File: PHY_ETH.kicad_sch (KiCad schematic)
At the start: 15 parts, among them U8 LAN8742A, Y1 LFXTAL071758Cutt

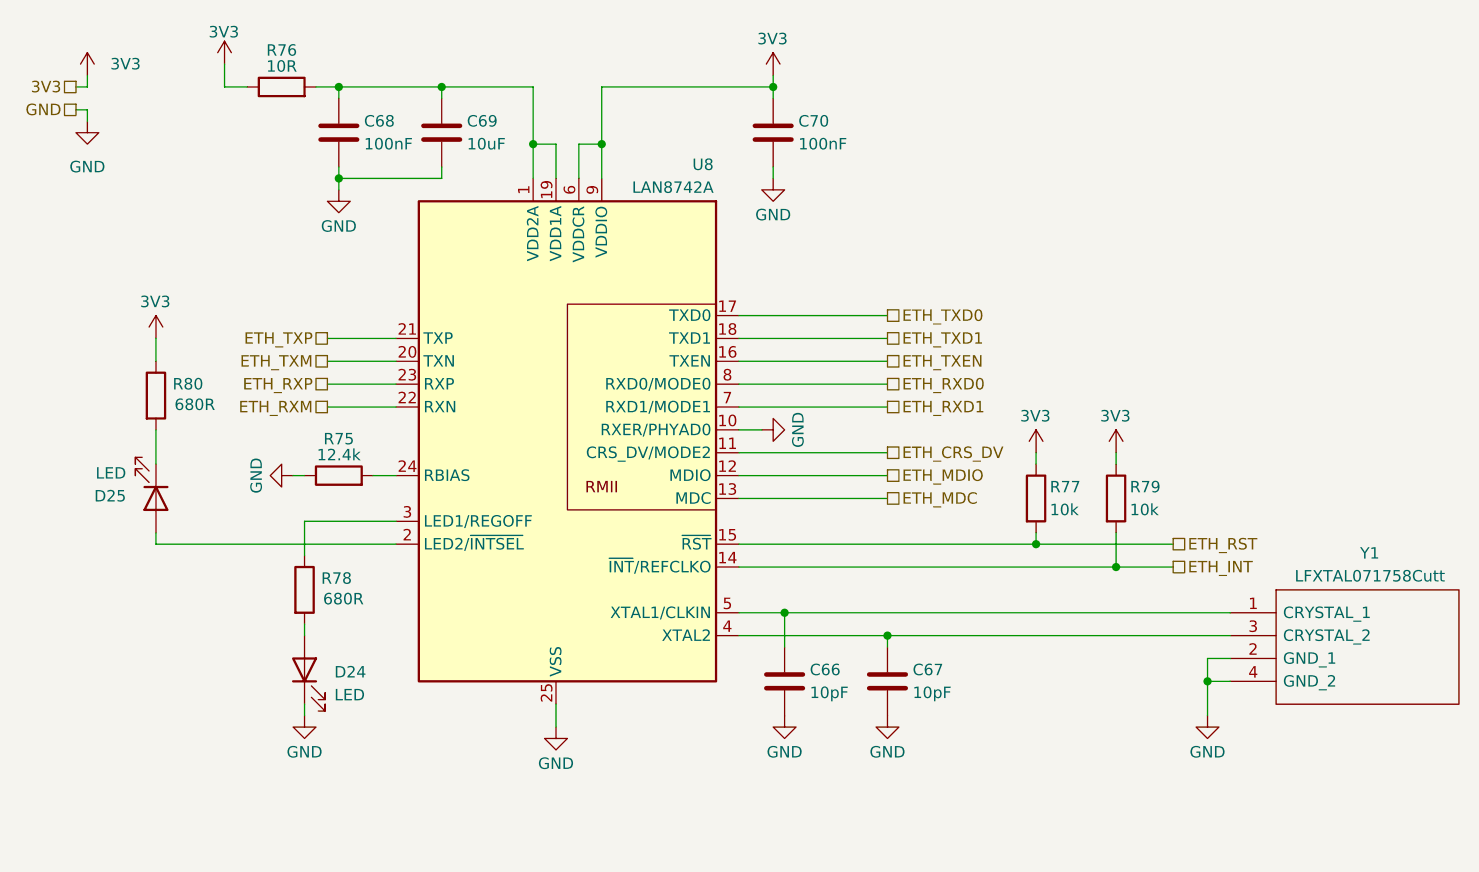
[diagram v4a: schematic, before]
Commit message: redid annotations, added test point
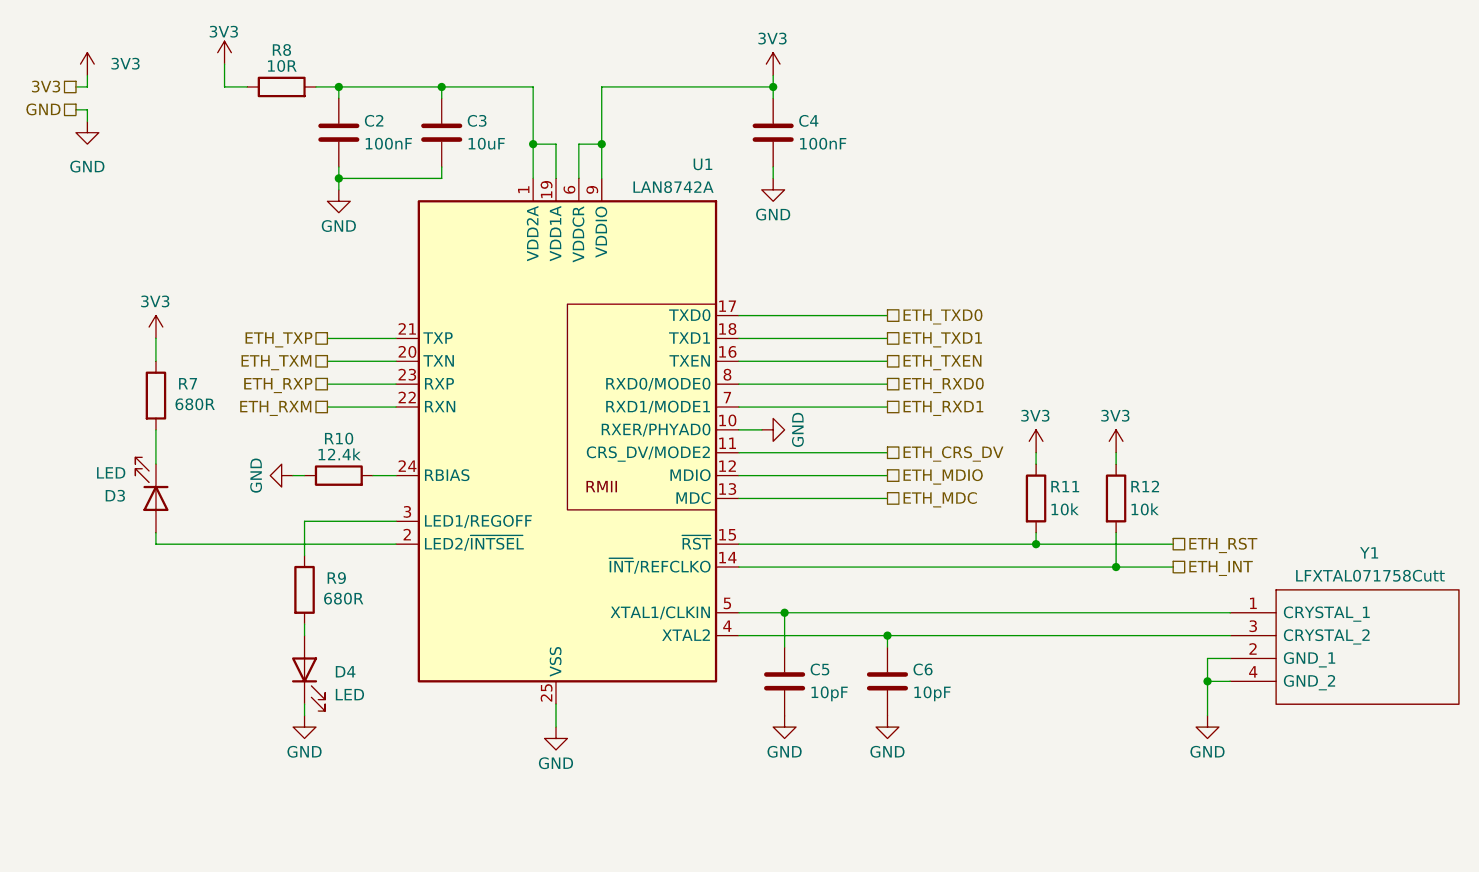
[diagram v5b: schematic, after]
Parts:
- C6: renamed from C67; footprint (none) -> Capacitor_SMD:C_0603_1608Metric_Pad1.08x0.95mm_HandSolder
- renumbered C68 to C2, C69 to C3, C70 to C4, C66 to C5, D25 to D3, D24 to D4, R75 to R10, R77 to R11, R79 to R12, R80 to R7, R76 to R8, R78 to R9, U8 to U1
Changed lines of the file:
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@@
 		(on_board yes)
 		(dnp no)
-		(property "Reference" "R79"
+		(property "Reference" "R12"
 			(at 142.494 69.85 0)
 			(effects
@@
 			(project "NCU"
 				(path "/3aee14c3-5480-4f7c-989e-3fef81779034/9758cbcc-2ab2-405c-935d-3964f8470771"
-					(reference "R79")
+					(reference "R12")
 					(unit 1)
 				)
@@
 		(on_board yes)
 		(dnp no)
-		(property "Reference" "R80"
+		(property "Reference" "R7"
 			(at 37.846 58.42 0)
 			(effects
@@
 			(project "NCU"
 				(path "/3aee14c3-5480-4f7c-989e-3fef81779034/9758cbcc-2ab2-405c-935d-3964f8470771"
-					(reference "R80")
+					(reference "R7")
 					(unit 1)
 				)
@@
 		(on_board yes)
 		(dnp no)
-		(property "Reference" "D24"
+		(property "Reference" "D4"
 			(at 54.102 90.424 90)
 			(effects
@@
 			(project "NCU"
 				(path "/3aee14c3-5480-4f7c-989e-3fef81779034/9758cbcc-2ab2-405c-935d-3964f8470771"
-					(reference "D24")
+					(reference "D4")
 					(unit 1)
 				)
@@
 		(on_board yes)
 		(dnp no)
-		(property "Reference" "R78"
+		(property "Reference" "R9"
 			(at 54.356 80.01 0)
 			(effects
@@
 			(project "NCU"
 				(path "/3aee14c3-5480-4f7c-989e-3fef81779034/9758cbcc-2ab2-405c-935d-3964f8470771"
-					(reference "R78")
+					(reference "R9")
 					(unit 1)
 				)
@@
 		(on_board yes)
 		(dnp no)
-		(property "Reference" "#PWR0237"
+		(property "Reference" "#PWR0100"
 			(at 151.13 101.6 0)
 			(effects
@@
 			(project "NCU"
 				(path "/3aee14c3-5480-4f7c-989e-3fef81779034/9758cbcc-2ab2-405c-935d-3964f8470771"
-					(reference "#PWR0237")
+					(reference "#PWR0100")
 					(unit 1)
 				)
@@
 		(on_board yes)
 		(dnp no)
-		(property "Reference" "C70"
+		(property "Reference" "C4"
 			(at 105.664 29.21 0)
 			(effects
@@
 			(project "NCU"
 				(path "/3aee14c3-5480-4f7c-989e-3fef81779034/9758cbcc-2ab2-405c-935d-3964f8470771"
-					(reference "C70")
+					(reference "C4")
 					(unit 1)
 				)
@@
 		(on_board yes)
 		(dnp no)
-		(property "Reference" "#PWR0241"
+		(property "Reference" "#PWR091"
 			(at 54.61 43.18 0)
 			(effects
@@
 			(project "NCU"
 				(path "/3aee14c3-5480-4f7c-989e-3fef81779034/9758cbcc-2ab2-405c-935d-3964f8470771"
-					(reference "#PWR0241")
+					(reference "#PWR091")
 					(unit 1)
 				)
@@
 		(on_board yes)
 		(dnp no)
-		(property "Reference" "#PWR0238"
+		(property "Reference" "#PWR096"
 			(at 104.14 101.6 0)
 			(effects
@@
 			(project "NCU"
 				(path "/3aee14c3-5480-4f7c-989e-3fef81779034/9758cbcc-2ab2-405c-935d-3964f8470771"
-					(reference "#PWR0238")
+					(reference "#PWR096")
 					(unit 1)
 				)
@@
 		(on_board yes)
 		(dnp no)
-		(property "Reference" "#PWR0240"
+		(property "Reference" "#PWR088"
 			(at 41.91 26.67 0)
 			(effects
@@
 			(project "NCU"
 				(path "/3aee14c3-5480-4f7c-989e-3fef81779034/9758cbcc-2ab2-405c-935d-3964f8470771"
-					(reference "#PWR0240")
+					(reference "#PWR088")
 					(unit 1)
 				)
@@
 		(on_board yes)
 		(dnp no)
-		(property "Reference" "#PWR0234"
+		(property "Reference" "#PWR092"
 			(at 78.74 102.87 0)
 			(effects
@@
 			(project "NCU"
 				(path "/3aee14c3-5480-4f7c-989e-3fef81779034/9758cbcc-2ab2-405c-935d-3964f8470771"
-					(reference "#PWR0234")
+					(reference "#PWR092")
 					(unit 1)
 				)
@@
 		(on_board yes)
 		(dnp no)
-		(property "Reference" "C68"
+		(property "Reference" "C2"
 			(at 57.404 29.21 0)
 			(effects
@@
 			(project "NCU"
 				(path "/3aee14c3-5480-4f7c-989e-3fef81779034/9758cbcc-2ab2-405c-935d-3964f8470771"
-					(reference "C68")
+					(reference "C2")
 					(unit 1)
 				)
@@
 		(on_board yes)
 		(dnp no)
-		(property "Reference" "C67"
+		(property "Reference" "C6"
 			(at 118.364 90.17 0)
 			(effects
@@
 			)
 		)
-		(property "Footprint" ""
+		(property "Footprint" "Capacitor_SMD:C_0603_1608Metric_Pad1.08x0.95mm_HandSolder"
 			(at 116.5352 95.25 0)
 			(effects
@@
 			(project "NCU"
 				(path "/3aee14c3-5480-4f7c-989e-3fef81779034/9758cbcc-2ab2-405c-935d-3964f8470771"
-					(reference "C67")
+					(reference "C6")
 					(unit 1)
 				)
@@
 		(on_board yes)
 		(dnp no)
-		(property "Reference" "U8"
+		(property "Reference" "U1"
 			(at 96.266 34.036 0)
 			(effects
@@
 			(project "NCU"
 				(path "/3aee14c3-5480-4f7c-989e-3fef81779034/9758cbcc-2ab2-405c-935d-3964f8470771"
-					(reference "U8")
+					(reference "U1")
 					(unit 1)
 				)
@@
 		(on_board yes)
 		(dnp no)
-		(property "Reference" "D25"
+		(property "Reference" "D3"
 			(at 30.988 70.866 90)
 			(effects
@@
 			(project "NCU"
 				(path "/3aee14c3-5480-4f7c-989e-3fef81779034/9758cbcc-2ab2-405c-935d-3964f8470771"
-					(reference "D25")
+					(reference "D3")
 					(unit 1)
 				)
@@
 		(on_board yes)
 		(dnp no)
-		(property "Reference" "R76"
+		(property "Reference" "R8"
 			(at 48.26 21.336 90)
 			(effects
@@
 			(project "NCU"
 				(path "/3aee14c3-5480-4f7c-989e-3fef81779034/9758cbcc-2ab2-405c-935d-3964f8470771"
-					(reference "R76")
+					(reference "R8")
 					(unit 1)
 				)
@@
 		(on_board yes)
 		(dnp no)
-		(property "Reference" "R77"
+		(property "Reference" "R11"
 			(at 133.604 69.85 0)
 			(effects
@@
 			(project ""
 				(path "/3aee14c3-5480-4f7c-989e-3fef81779034/9758cbcc-2ab2-405c-935d-3964f8470771"
-					(reference "R77")
+					(reference "R11")
 					(unit 1)
 				)
@@
 		(on_board yes)
 		(dnp no)
-		(property "Reference" "C69"
+		(property "Reference" "C3"
 			(at 68.834 29.21 0)
 			(effects
@@
 			(project "NCU"
 				(path "/3aee14c3-5480-4f7c-989e-3fef81779034/9758cbcc-2ab2-405c-935d-3964f8470771"
-					(reference "C69")
+					(reference "C3")
 					(unit 1)
 				)
@@
 		(on_board yes)
 		(dnp no)
-		(property "Reference" "#PWR0242"
+		(property "Reference" "#PWR098"
 			(at 132.08 69.85 0)
 			(effects
@@
 			(project "NCU"
 				(path "/3aee14c3-5480-4f7c-989e-3fef81779034/9758cbcc-2ab2-405c-935d-3964f8470771"
-					(reference "#PWR0242")
+					(reference "#PWR098")
 					(unit 1)
 				)
@@
 		(on_board yes)
 		(dnp no)
-		(property "Reference" "#PWR0243"
+		(property "Reference" "#PWR090"
 			(at 50.8 101.6 0)
 			(effects
@@
 			(project "NCU"
 				(path "/3aee14c3-5480-4f7c-989e-3fef81779034/9758cbcc-2ab2-405c-935d-3964f8470771"
-					(reference "#PWR0243")
+					(reference "#PWR090")
 					(unit 1)
 				)
@@
 		(on_board yes)
 		(dnp no)
-		(property "Reference" "#PWR0244"
+		(property "Reference" "#PWR099"
 			(at 140.97 69.85 0)
 			(effects
@@
 			(project "NCU"
 				(path "/3aee14c3-5480-4f7c-989e-3fef81779034/9758cbcc-2ab2-405c-935d-3964f8470771"
-					(reference "#PWR0244")
+					(reference "#PWR099")
 					(unit 1)
 				)
@@
 		(dnp no)
 		(fields_autoplaced yes)
-		(property "Reference" "#PWR0115"
+		(property "Reference" "#PWR086"
 			(at 26.67 35.56 0)
 			(effects
@@
 			(project "NCU"
 				(path "/3aee14c3-5480-4f7c-989e-3fef81779034/9758cbcc-2ab2-405c-935d-3964f8470771"
-					(reference "#PWR0115")
+					(reference "#PWR086")
 					(unit 1)
 				)
@@
 		(on_board yes)
 		(dnp no)
-		(property "Reference" "#PWR0235"
+		(property "Reference" "#PWR094"
 			(at 102.87 27.94 0)
 			(effects
@@
 			(project "NCU"
 				(path "/3aee14c3-5480-4f7c-989e-3fef81779034/9758cbcc-2ab2-405c-935d-3964f8470771"
-					(reference "#PWR0235")
+					(reference "#PWR094")
 					(unit 1)
 				)
@@
 		(on_board yes)
 		(dnp no)
-		(property "Reference" "#PWR0246"
+		(property "Reference" "#PWR087"
 			(at 34.29 57.15 0)
 			(effects
@@
 			(project "NCU"
 				(path "/3aee14c3-5480-4f7c-989e-3fef81779034/9758cbcc-2ab2-405c-935d-3964f8470771"
-					(reference "#PWR0246")
+					(reference "#PWR087")
 					(unit 1)
 				)
@@
 		(on_board yes)
 		(dnp no)
-		(property "Reference" "#PWR0236"
+		(property "Reference" "#PWR089"
 			(at 43.18 68.58 0)
 			(effects
@@
 			(project "NCU"
 				(path "/3aee14c3-5480-4f7c-989e-3fef81779034/9758cbcc-2ab2-405c-935d-3964f8470771"
-					(reference "#PWR0236")
+					(reference "#PWR089")
 					(unit 1)
 				)
@@
 		(on_board yes)
 		(dnp no)
-		(property "Reference" "#PWR047"
+		(property "Reference" "#PWR093"
 			(at 107.95 63.5 0)
 			(effects
@@
 			(project "NCU"
 				(path "/3aee14c3-5480-4f7c-989e-3fef81779034/9758cbcc-2ab2-405c-935d-3964f8470771"
-					(reference "#PWR047")
+					(reference "#PWR093")
 					(unit 1)
 				)
@@
 		(on_board yes)
 		(dnp no)
-		(property "Reference" "C66"
+		(property "Reference" "C5"
 			(at 106.934 90.17 0)
 			(effects
@@
 			(project ""
 				(path "/3aee14c3-5480-4f7c-989e-3fef81779034/9758cbcc-2ab2-405c-935d-3964f8470771"
-					(reference "C66")
+					(reference "C5")
 					(unit 1)
 				)
@@
 		(on_board yes)
 		(dnp no)
-		(property "Reference" "#PWR0245"
+		(property "Reference" "#PWR095"
 			(at 102.87 41.91 0)
 			(effects
@@
 			(project "NCU"
 				(path "/3aee14c3-5480-4f7c-989e-3fef81779034/9758cbcc-2ab2-405c-935d-3964f8470771"
-					(reference "#PWR0245")
+					(reference "#PWR095")
 					(unit 1)
 				)
@@
 		(dnp no)
 		(fields_autoplaced yes)
-		(property "Reference" "#PWR0114"
+		(property "Reference" "#PWR085"
 			(at 26.67 27.94 0)
 			(effects
@@
 			(project "NCU"
 				(path "/3aee14c3-5480-4f7c-989e-3fef81779034/9758cbcc-2ab2-405c-935d-3964f8470771"
-					(reference "#PWR0114")
+					(reference "#PWR085")
 					(unit 1)
 				)
@@
 		(on_board yes)
 		(dnp no)
-		(property "Reference" "#PWR0239"
+		(property "Reference" "#PWR097"
 			(at 115.57 101.6 0)
 			(effects
@@
 			(project "NCU"
 				(path "/3aee14c3-5480-4f7c-989e-3fef81779034/9758cbcc-2ab2-405c-935d-3964f8470771"
-					(reference "#PWR0239")
+					(reference "#PWR097")
 					(unit 1)
 				)
@@
 		(on_board yes)
 		(dnp no)
-		(property "Reference" "R75"
+		(property "Reference" "R10"
 			(at 54.61 64.516 90)
 			(effects
@@
 			(project ""
 				(path "/3aee14c3-5480-4f7c-989e-3fef81779034/9758cbcc-2ab2-405c-935d-3964f8470771"
-					(reference "R75")
-					(unit 1)
-				)
+					(reference "R10")
+					(unit 1)
+				)
